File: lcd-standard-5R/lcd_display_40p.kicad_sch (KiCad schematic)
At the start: 36 parts, among them J5 Conn_01x06_MountingPin, J6 Conn_01x40_MountingPin, U7 XPT2046TS, U8 TPS61169

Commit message: Change MCU to STM32H743
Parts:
- added RN1, RN2, RN3, RN4, RN5, RN6, RN7: 50, Resistor_SMD:R_Array_Convex_4x0402, symbol Device:R_Pack04
- added RN8, RN9: 10K, Resistor_SMD:R_Array_Convex_4x0402, symbol Device:R_Pack04
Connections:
- net GND: now also RN8.5 (R4.2), RN8.6 (R3.2), RN8.7 (R2.2), RN8.8 (R1.2), RN9.5 (R4.2), RN9.6 (R3.2), RN9.7 (R2.2), RN9.8 (R1.2)
- net LCD_B0: now also RN3.8 (R1.2); no longer J6.20 (Pin_20)
- net LCD_B1: now also RN3.7 (R2.2); no longer J6.19 (Pin_19)
- net LCD_B2: now also RN3.6 (R3.2); no longer J6.18 (Pin_18)
- net LCD_B3: now also RN3.5 (R4.2); no longer J6.17 (Pin_17)
- net LCD_B4: now also RN2.8 (R1.2); no longer J6.16 (Pin_16)
- net LCD_B5: now also RN2.7 (R2.2); no longer J6.15 (Pin_15)
- net LCD_B6: now also RN2.6 (R3.2); no longer J6.14 (Pin_14)
- net LCD_B7: now also RN2.5 (R4.2); no longer J6.13 (Pin_13)
- net LCD_CLK: now also RN1.4 (R4.1); no longer J6.11 (Pin_11)
- net LCD_DE: now also RN1.1 (R1.1); no longer J6.7 (Pin_7)
- net LCD_G0: now also RN5.8 (R1.2); no longer J6.28 (Pin_28)
- net LCD_G1: now also RN5.7 (R2.2); no longer J6.27 (Pin_27)
- net LCD_G2: now also RN5.6 (R3.2); no longer J6.26 (Pin_26)
- net LCD_G3: now also RN5.5 (R4.2); no longer J6.25 (Pin_25)
- net LCD_G4: now also RN4.8 (R1.2); no longer J6.24 (Pin_24)
- net LCD_G5: now also RN4.7 (R2.2); no longer J6.23 (Pin_23)
- net LCD_G6: now also RN4.6 (R3.2); no longer J6.22 (Pin_22)
- net LCD_G7: now also RN4.5 (R4.2); no longer J6.21 (Pin_21)
- net LCD_HSYNC: now also RN1.3 (R3.1); no longer J6.9 (Pin_9)
- net LCD_R0: now also RN7.8 (R1.2); no longer J6.36 (Pin_36)
- net LCD_R1: now also RN7.7 (R2.2); no longer J6.35 (Pin_35)
- net LCD_R2: now also RN7.6 (R3.2); no longer J6.34 (Pin_34)
- net LCD_R3: now also RN7.5 (R4.2); no longer J6.33 (Pin_33)
- net LCD_R4: now also RN6.8 (R1.2); no longer J6.32 (Pin_32)
- net LCD_R5: now also RN6.7 (R2.2); no longer J6.31 (Pin_31)
- net LCD_R6: now also RN6.6 (R3.2); no longer J6.30 (Pin_30)
- net LCD_R7: now also RN6.5 (R4.2); no longer J6.29 (Pin_29)
- net LCD_VSYNC: now also RN1.2 (R2.1); no longer J6.8 (Pin_8)
- net TP_BUSY renamed RTP_BUSY
- net TP_CLK renamed RTP_CLK
- net TP_CS renamed RTP_CS
- net TP_INT renamed CTP_INT
- net TP_IRQ renamed RTP_IRQ
- net TP_MISO renamed RTP_MISO
- net TP_MOSI renamed RTP_MOSI
- net TP_SCL renamed CTP_SCL
- net TP_SDA renamed CTP_SDA
- net TP_WAKE renamed CTP_WAKE
- new net: J6.33 (Pin_33), RN7.4 (R4.1)
- new net: J6.16 (Pin_16), RN2.1 (R1.1)
- new net: J6.15 (Pin_15), RN2.2 (R2.1)
- new net: J6.14 (Pin_14), RN2.3 (R3.1)
- new net: J6.13 (Pin_13), RN2.4 (R4.1)
- new net: J6.11 (Pin_11), RN1.5 (R4.2)
- new net: J6.9 (Pin_9), RN1.6 (R3.2)
- new net: J6.8 (Pin_8), RN1.7 (R2.2)
- new net: J6.7 (Pin_7), RN1.8 (R1.2)
- new net: J6.17 (Pin_17), RN3.4 (R4.1)
- new net: J6.21 (Pin_21), RN4.4 (R4.1)
- new net: J6.22 (Pin_22), RN4.3 (R3.1)
- new net: J6.23 (Pin_23), RN4.2 (R2.1)
- new net: J6.24 (Pin_24), RN4.1 (R1.1)
- new net: J6.25 (Pin_25), RN5.4 (R4.1)
- new net: J6.26 (Pin_26), RN5.3 (R3.1)
- new net: J6.29 (Pin_29), RN6.4 (R4.1)
- new net: J6.30 (Pin_30), RN6.3 (R3.1)
- new net: J6.31 (Pin_31), RN6.2 (R2.1)
- new net: J6.32 (Pin_32), RN6.1 (R1.1)
- new net B0: J6.20 (Pin_20), RN3.1 (R1.1), RN9.3 (R3.1)
- new net B1: J6.19 (Pin_19), RN3.2 (R2.1), RN9.2 (R2.1)
- new net B2: J6.18 (Pin_18), RN3.3 (R3.1), RN9.1 (R1.1)
- new net G0: J6.28 (Pin_28), RN5.1 (R1.1), RN8.1 (R1.1)
- new net G1: J6.27 (Pin_27), RN5.2 (R2.1), RN9.4 (R4.1)
- new net R0: J6.36 (Pin_36), RN7.1 (R1.1), RN8.4 (R4.1)
- new net R1: J6.35 (Pin_35), RN7.2 (R2.1), RN8.3 (R3.1)
- new net R2: J6.34 (Pin_34), RN7.3 (R3.1), RN8.2 (R2.1)
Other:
- moved on the sheet: J6, R19, R20, R23, R27

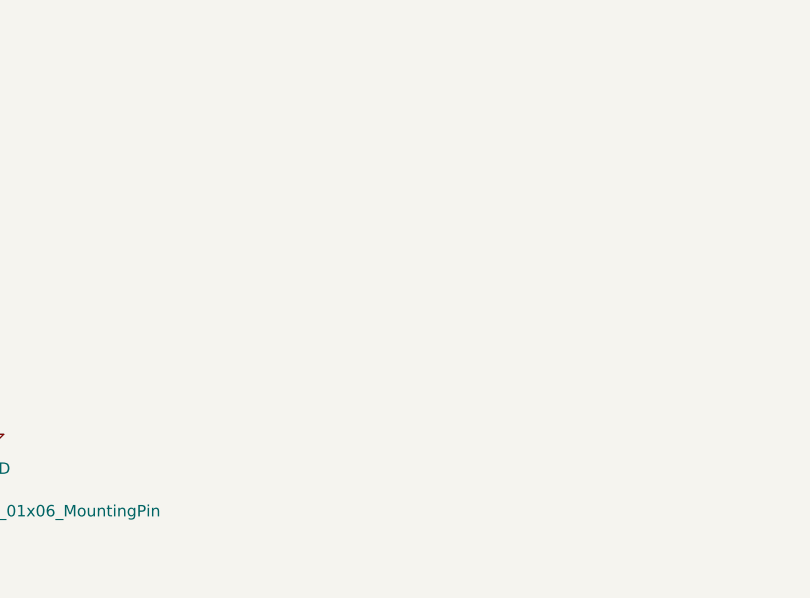
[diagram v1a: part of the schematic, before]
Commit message: Add 10P FPC for 5-inch Tailor pixel CTP
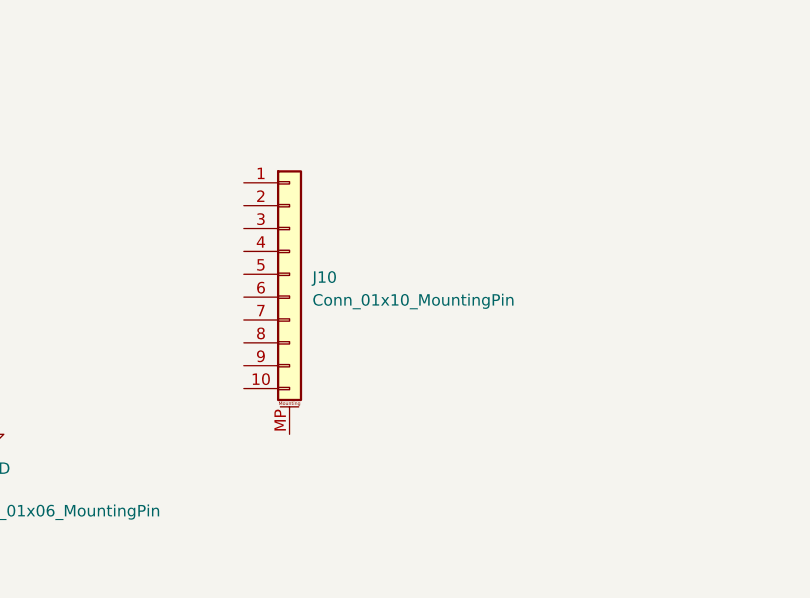
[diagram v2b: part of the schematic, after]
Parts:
- added J10: Conn_01x10_MountingPin, Connector_FFC-FPC:Molex_54548-1071_1x10-1MP_P0.5mm_Horizontal, symbol Connector_Generic_MountingPin:Conn_01x10_MountingPin
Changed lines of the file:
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@@
+	)
+	(symbol
+		(lib_id "Connector_Generic_MountingPin:Conn_01x10_MountingPin")
+		(at 193.04 142.24 0)
+		(unit 1)
+		(exclude_from_sim no)
+		(in_bom yes)
+		(on_board yes)
+		(dnp no)
+		(fields_autoplaced yes)
+		(property "Reference" "J10"
+			(at 195.58 142.5955 0)
+			(effects
+				(font
+					(size 1.27 1.27)
+				)
+				(justify left)
+			)
+		)
+		(property "Value" "Conn_01x10_MountingPin"
+			(at 195.58 145.1355 0)
+			(effects
+				(font
+					(size 1.27 1.27)
+				)
+				(justify left)
+			)
+		)
+		(property "Footprint" "Connector_FFC-FPC:Molex_54548-1071_1x10-1MP_P0.5mm_Horizontal"
+			(at 193.04 142.24 0)
+			(effects
+				(font
+					(size 1.27 1.27)
+				)
+				(hide yes)
+			)
+		)
+		(property "Datasheet" "~"
+			(at 193.04 142.24 0)
+			(effects
+				(font
+					(size 1.27 1.27)
+				)
+				(hide yes)
+			)
+		)
+		(property "Description" "Generic connectable mounting pin connector, single row, 01x10, script generated (kicad-library-utils/schlib/autogen/connector/)"
+			(at 193.04 142.24 0)
+			(effects
+				(font
+					(size 1.27 1.27)
+				)
+				(hide yes)
+			)
+		)
+		(pin "5"
+		)
+		(pin "MP"
+		)
+		(pin "6"
+		)
+		(pin "1"
+		)
+		(pin "2"
+		)
+		(pin "8"
+		)
+		(pin "7"
+		)
+		(pin "10"
+		)
+		(pin "4"
+		)
+		(pin "3"
+		)
+		(pin "9"
+		)
+		(instances
+			(project ""
+				(path "/a9fe5be7-3a80-455e-a721-d53819db4a52/d9588482-1ca8-4134-8583-2eaba9a5f5dc"
+					(reference "J10")
+					(unit 1)
+				)
+			)
+		)
 	)
 	(symbol

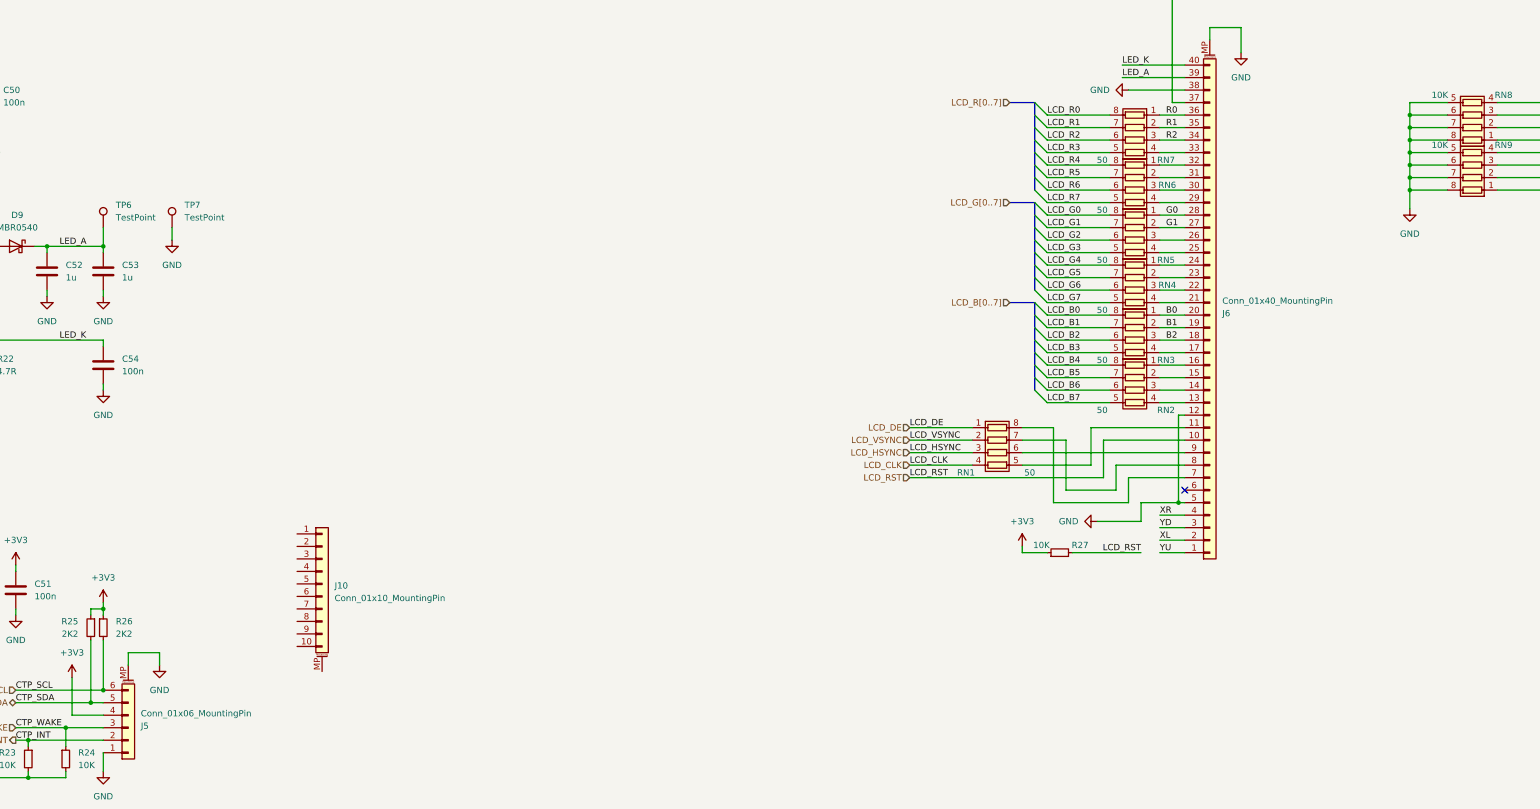
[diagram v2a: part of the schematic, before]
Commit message: Change 10P CTP to omron type
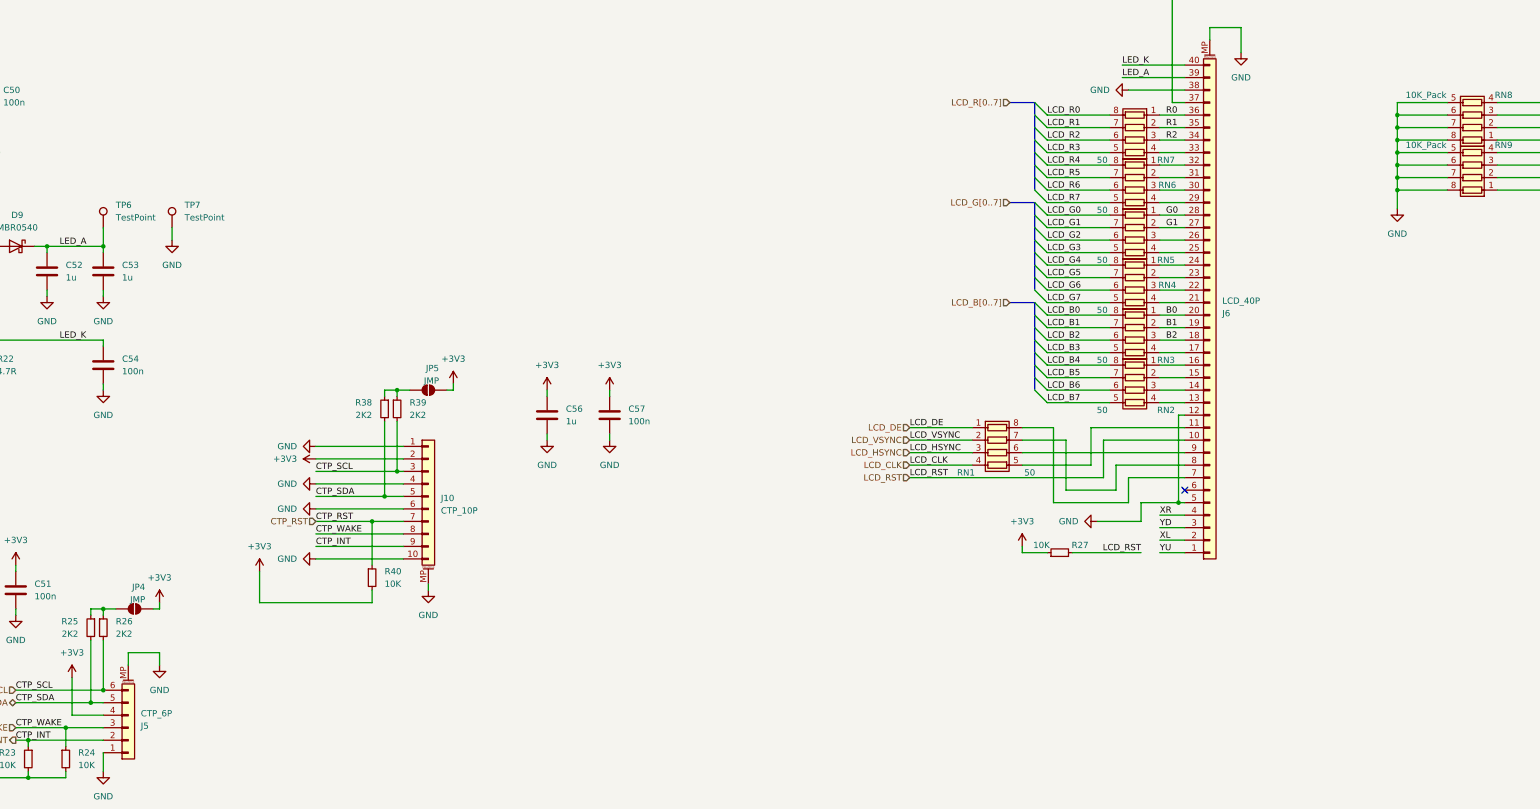
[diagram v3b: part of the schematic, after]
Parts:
- added C56: 1u, Capacitor_SMD:C_0603_1608Metric, symbol Device:C
- added C57: 100n, Capacitor_SMD:C_0402_1005Metric, symbol Device:C
- added JP4, JP5: JMP, Jumper:SolderJumper-2_P1.3mm_Open_RoundedPad1.0x1.5mm, symbol Jumper:SolderJumper_2_Open
- added R38, R39: 2K2, Resistor_SMD:R_0402_1005Metric, symbol Device:R_Small
- added R40: 10K, Resistor_SMD:R_0402_1005Metric, symbol Device:R_Small
- C42, C43, C44, C45, C46, C50, C51, C54: JLCPCB Part # C1525 -> C307331
- J10: value Conn_01x10_MountingPin -> CTP_10P; footprint Connector_FFC-FPC:Molex_54548-1071_1x10-1MP_P0.5mm_Horizontal -> Connector_FPC:Conn_FPC_10P_0.5mm_OMRON_XF2M-1015-1A; JLCPCB Part # (none) -> C271735
- J5: value Conn_01x06_MountingPin -> CTP_6P
- J6: value Conn_01x40_MountingPin -> LCD_40P
- RN8, RN9: value 10K -> 10K_Pack; JLCPCB Part # C48442 -> C25725
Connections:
- net +3V3: now also J10.2 (Pin_2), C56.1, C57.1, JP4.2 (B), JP5.2 (B), R40.2; no longer R25.1, R26.1
- net CTP_INT: now also J10.9 (Pin_9)
- net CTP_SCL: now also J10.3 (Pin_3), R39.2
- net CTP_SDA: now also J10.5 (Pin_5), R38.2
- net CTP_WAKE: now also J10.8 (Pin_8)
- net GND: now also J10.1 (Pin_1), J10.10 (Pin_10), J10.4 (Pin_4), J10.6 (Pin_6), J10.MP (MountPin), C56.2, C57.2
- net CTP_RST: now reaches J10.7 (Pin_7)
- net CTP_RST: now also R40.1
- new net: JP4.1 (A), R25.1, R26.1
- new net: JP5.1 (A), R38.1, R39.1
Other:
- moved on the sheet: J10

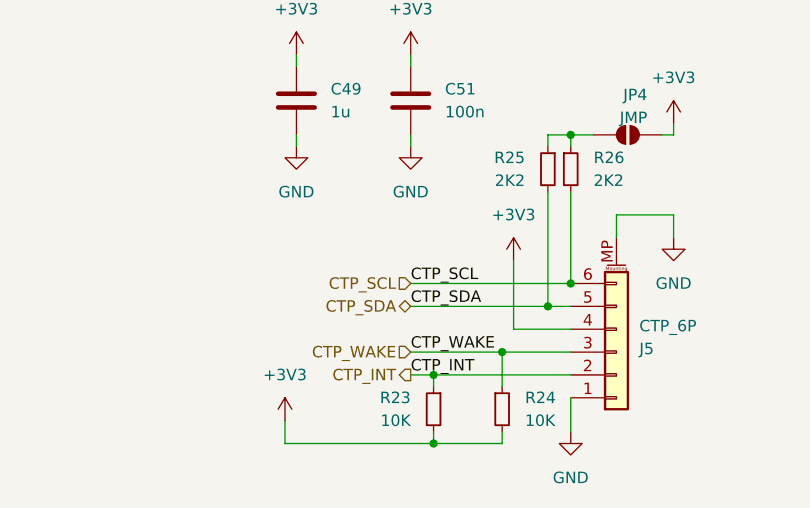
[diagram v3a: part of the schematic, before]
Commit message: Finished SDRAM, LCD (need checkup with CubeIDE), RTP touch controll
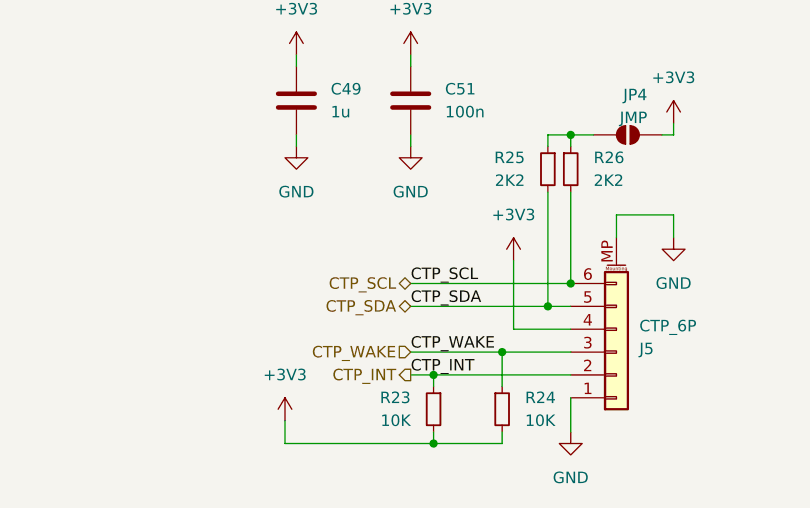
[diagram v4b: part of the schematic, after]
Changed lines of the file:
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@@
 	)
 	(hierarchical_label "CTP_SCL"
-		(shape input)
+		(shape bidirectional)
 		(at 130.81 163.83 180)
 		(fields_autoplaced yes)

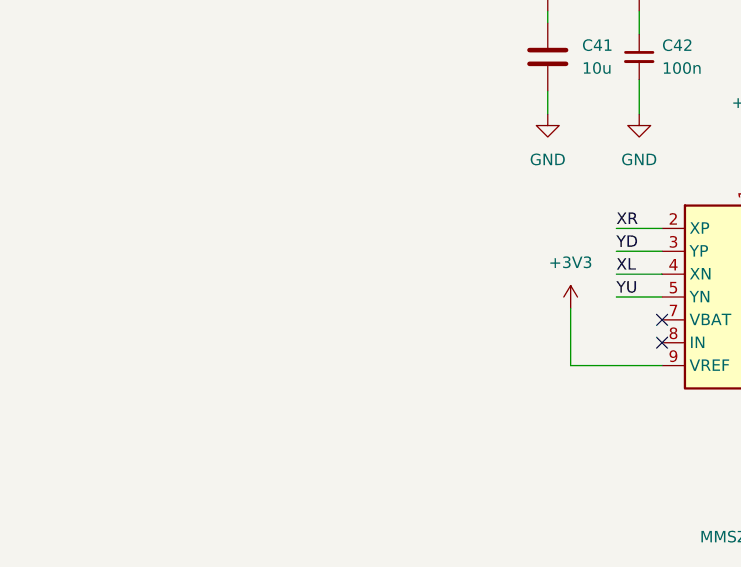
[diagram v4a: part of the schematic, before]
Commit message: Adding filter on MAX98357, TODO: Add more grounding vias
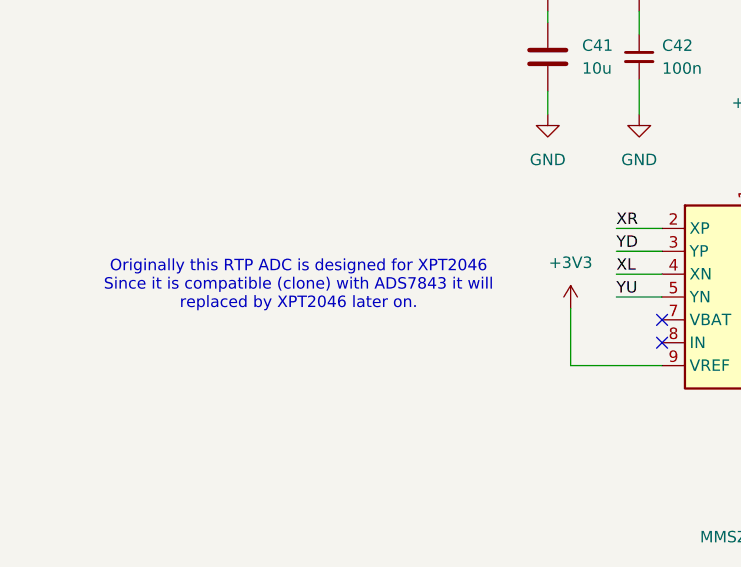
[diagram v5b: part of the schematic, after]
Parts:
- U7: JLCPCB Part # (none) -> C364888; now in the parts list
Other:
- note added: "Originally this RTP ADC is designed for XPT2046 Since it is compatible (clone) with ADS7843 it will replaced by XPT2046 later on."
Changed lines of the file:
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@@
 		)
 	)
+	(text "Originally this RTP ADC is designed for XPT2046\nSince it is compatible (clone) with ADS7843 it will\nreplaced by XPT2046 later on."
+		(exclude_from_sim no)
+		(at -91.186 80.01 0)
+		(effects
+			(font
+				(size 1.27 1.27)
+			)
+		)
+	)
 	(text "45mA"
 		(exclude_from_sim no)
@@
 		(unit 1)
 		(exclude_from_sim no)
-		(in_bom no)
+		(in_bom yes)
 		(on_board yes)
 		(dnp no)
@@
 			)
 		)
-		(property "JLCPCB Part #" ""
+		(property "JLCPCB Part #" "C364888"
 			(at -38.1 81.28 0)
 			(effects
